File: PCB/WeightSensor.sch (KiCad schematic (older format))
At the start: 2 parts

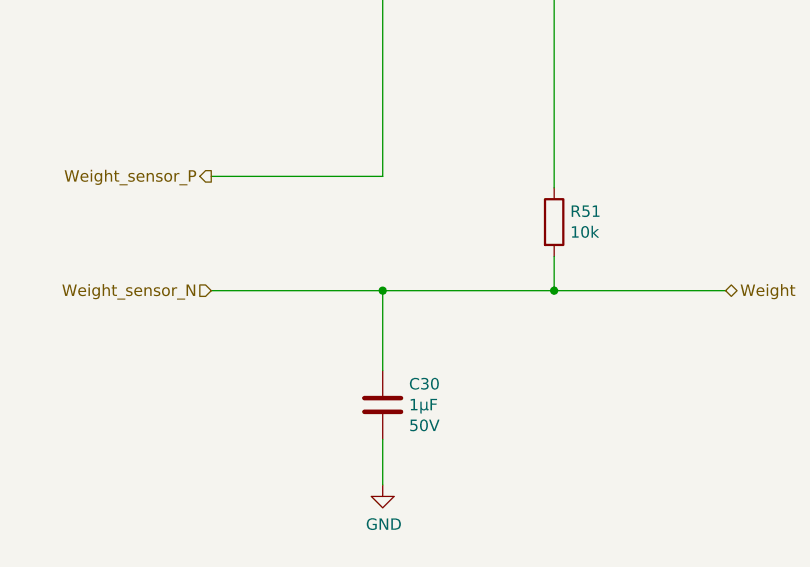
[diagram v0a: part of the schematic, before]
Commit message: Add support for the hall sensors and dome LED
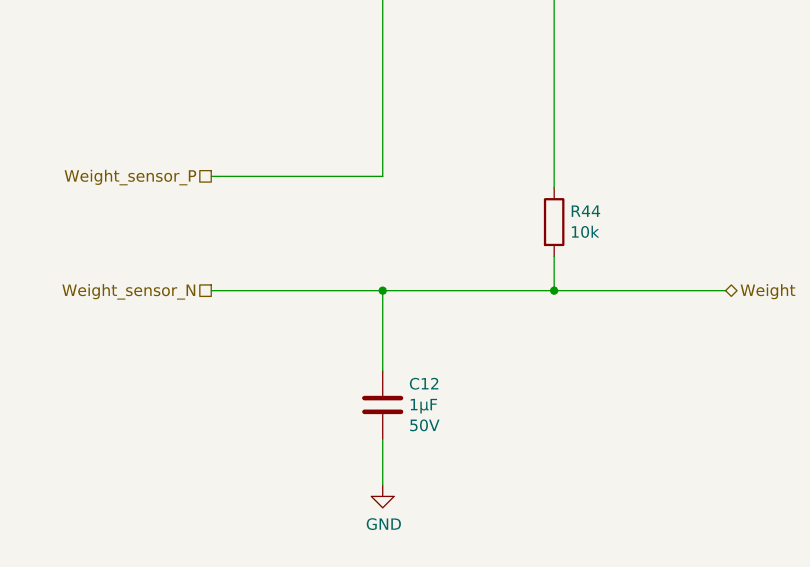
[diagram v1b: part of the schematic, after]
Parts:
- renumbered C30 to C12, R51 to R44
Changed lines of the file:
@@
 $Descr A4 11693 8268
 encoding utf-8
-Sheet 20 20
+Sheet 17 22
 Title "Litter Robot 3 - Weight sensor"
-Date "2021-04-02"
+Date "2021-04-03"
 Rev "A1"
 Comp "L. Sartory"
@@
 Comment4 ""
 $EndDescr
-Text HLabel 5000 4000 0    50   Input ~ 0
+Text HLabel 5000 4000 0    50   UnSpc ~ 0
 Weight_sensor_N
 $Comp
@@
 AR Path="/603F1DCE/606BBD2A" Ref="#PWR?"  Part="1"
 AR Path="/60624089/606BBD2A" Ref="#PWR?"  Part="1"
-AR Path="/606A580A/606BBD2A" Ref="#PWR0113"  Part="1"
-F 0 "#PWR0113" H 5750 4600 50  0001 C CNN
+AR Path="/606A580A/606BBD2A" Ref="#PWR071"  Part="1"
+F 0 "#PWR071" H 5750 4600 50  0001 C CNN
 F 1 "GND" H 5755 4677 50  0000 C CNN
 F 2 "" H 5750 4850 50  0001 C CNN
@@
 AR Path="/603F1DCE/606BBD37" Ref="R?"  Part="1"
 AR Path="/60624089/606BBD37" Ref="R?"  Part="1"
-AR Path="/606A580A/606BBD37" Ref="R51"  Part="1"
-F 0 "R51" H 6570 3746 50  0000 L CNN
+AR Path="/606A580A/606BBD37" Ref="R44"  Part="1"
+F 0 "R44" H 6570 3746 50  0000 L CNN
 F 1 "10k" H 6570 3655 50  0000 L CNN
 F 2 "Resistor_SMD:R_0603_1608Metric" V 6430 3700 50  0001 C CNN
@@
 Text HLabel 7250 4000 2    50   3State ~ 0
 Weight
-Text HLabel 5000 3500 0    50   Output ~ 0
+Text HLabel 5000 3500 0    50   UnSpc ~ 0
 Weight_sensor_P
 Text Notes 750  7500 0    50   ~ 0
@@
 AR Path="/603F1DCE/60701378" Ref="C?"  Part="1"
 AR Path="/60624089/60701378" Ref="C?"  Part="1"
-AR Path="/606A580A/60701378" Ref="C30"  Part="1"
-F 0 "C30" H 5865 4591 50  0000 L CNN
+AR Path="/606A580A/60701378" Ref="C12"  Part="1"
+F 0 "C12" H 5865 4591 50  0000 L CNN
 F 1 "1µF" H 5865 4500 50  0000 L CNN
 F 2 "Capacitor_SMD:C_0603_1608Metric" H 5788 4350 50  0001 C CNN

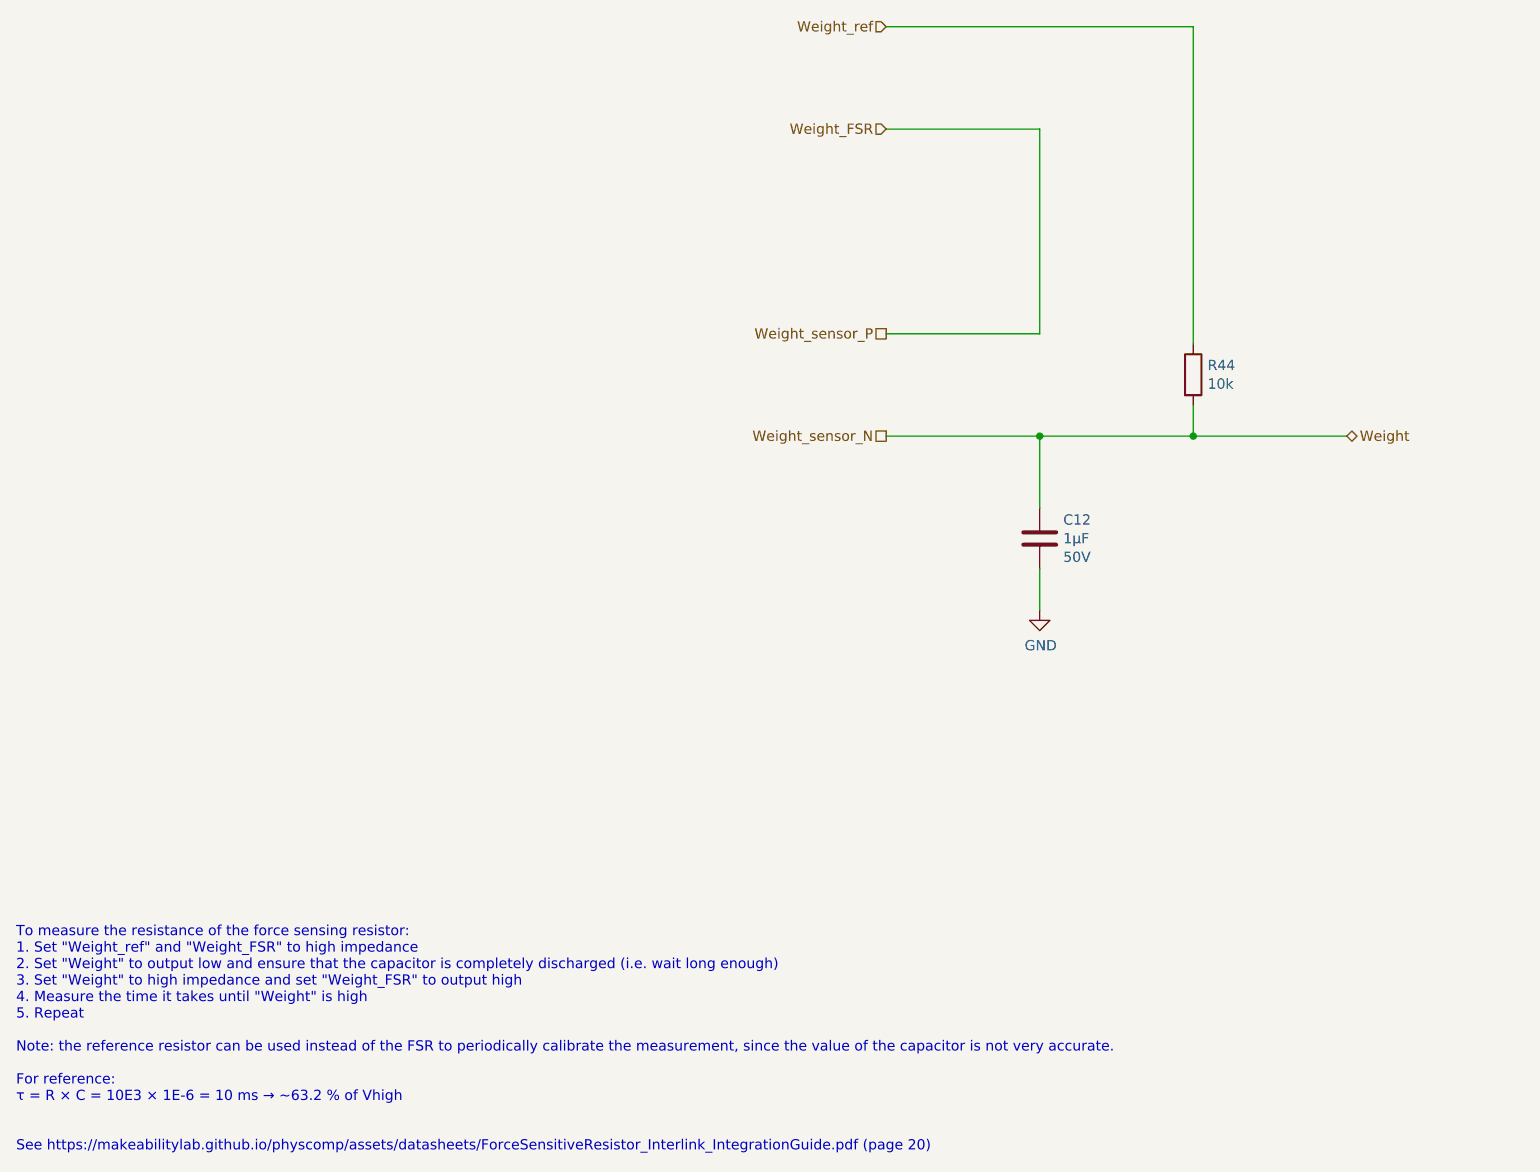
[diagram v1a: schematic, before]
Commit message: Reduce the weight sensor capacitor value
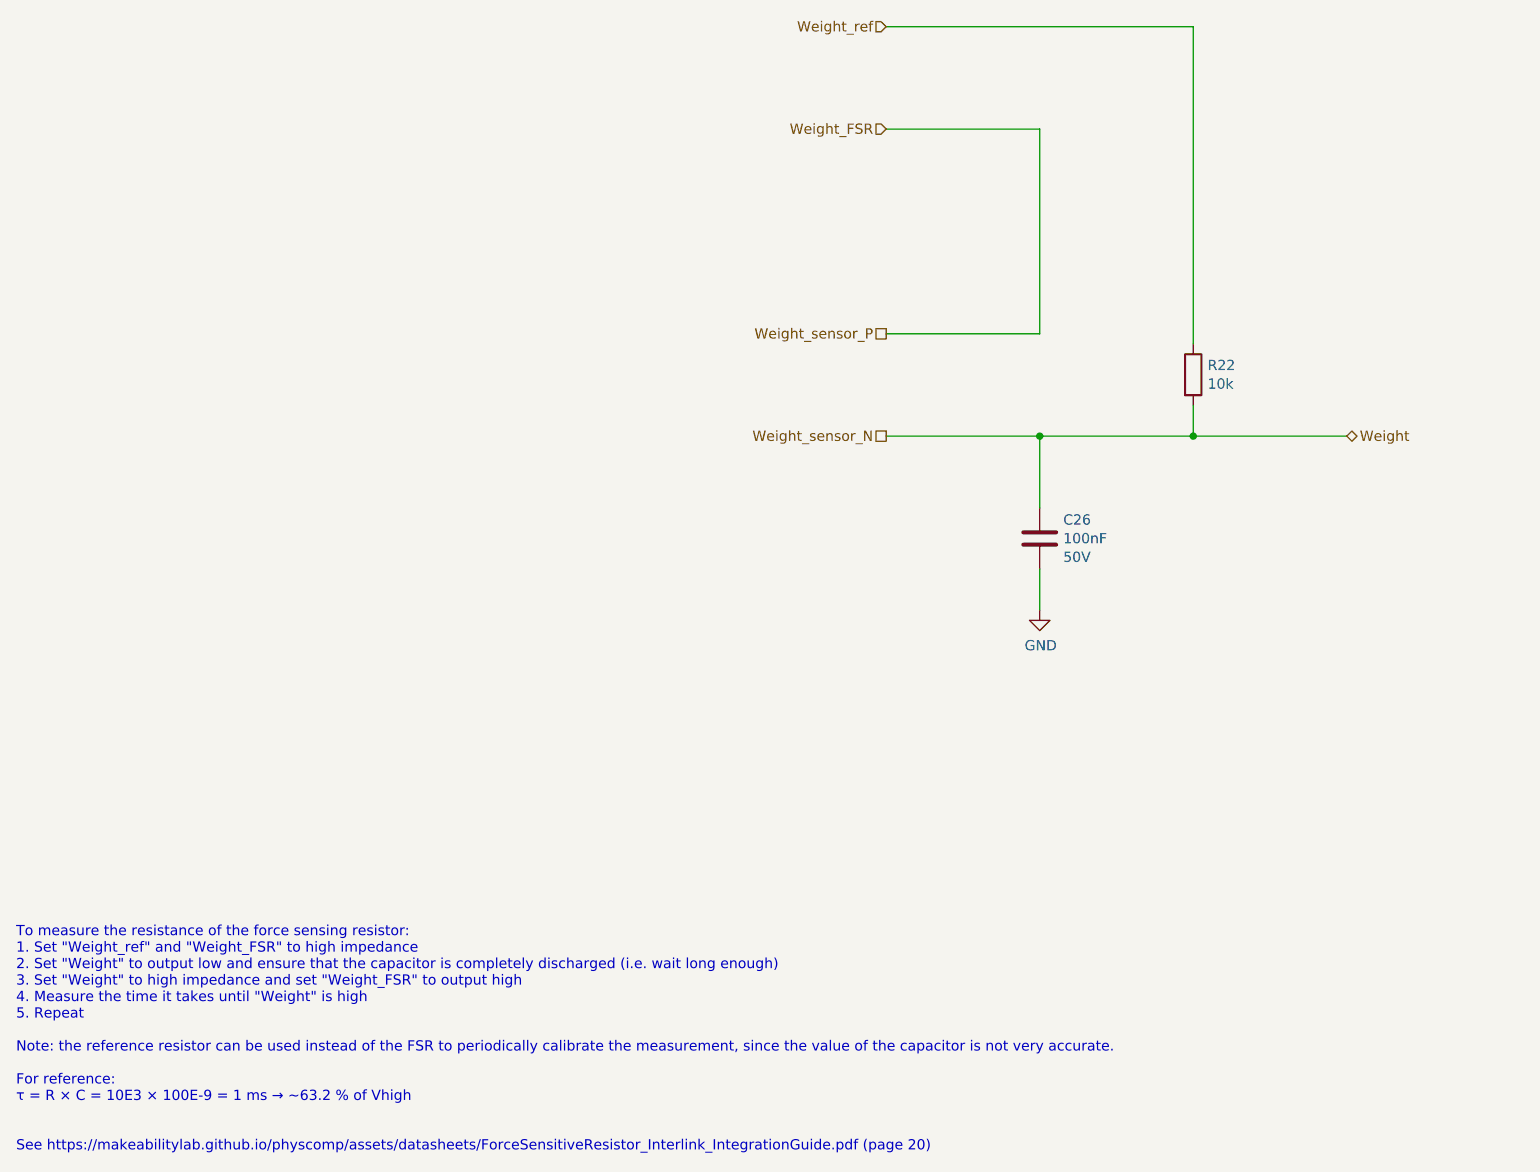
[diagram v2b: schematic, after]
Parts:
- removed C12: 1µF, Capacitor_SMD:C_0603_1608Metric, symbol Device:C
- added C26: 100nF, Capacitor_SMD:C_0603_1608Metric, symbol Device:C
- renumbered R44 to R22
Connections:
- net GND: now also C26.2
- net Weight: now also C26.1
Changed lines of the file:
@@
 $Descr A4 11693 8268
 encoding utf-8
-Sheet 17 22
+Sheet 6 22
 Title "Litter Robot 3 - Weight sensor"
-Date "2021-04-03"
+Date "2021-04-05"
 Rev "A1"
 Comp "L. Sartory"
@@
 AR Path="/603F1DCE/606BBD2A" Ref="#PWR?"  Part="1"
 AR Path="/60624089/606BBD2A" Ref="#PWR?"  Part="1"
-AR Path="/606A580A/606BBD2A" Ref="#PWR071"  Part="1"
-F 0 "#PWR071" H 5750 4600 50  0001 C CNN
+AR Path="/606A580A/606BBD2A" Ref="#PWR070"  Part="1"
+F 0 "#PWR070" H 5750 4600 50  0001 C CNN
 F 1 "GND" H 5755 4677 50  0000 C CNN
 F 2 "" H 5750 4850 50  0001 C CNN
@@
 AR Path="/603F1DCE/606BBD37" Ref="R?"  Part="1"
 AR Path="/60624089/606BBD37" Ref="R?"  Part="1"
-AR Path="/606A580A/606BBD37" Ref="R44"  Part="1"
-F 0 "R44" H 6570 3746 50  0000 L CNN
+AR Path="/606A580A/606BBD37" Ref="R22"  Part="1"
+F 0 "R22" H 6570 3746 50  0000 L CNN
 F 1 "10k" H 6570 3655 50  0000 L CNN
 F 2 "Resistor_SMD:R_0603_1608Metric" V 6430 3700 50  0001 C CNN
@@
 Weight_sensor_P
 Text Notes 750  7500 0    50   ~ 0
-To measure the resistance of the force sensing resistor:\n1. Set "Weight_ref" and "Weight_FSR" to high impedance\n2. Set "Weight" to output low and ensure that the capacitor is completely discharged (i.e. wait long enough)\n3. Set "Weight" to high impedance and set "Weight_FSR" to output high\n4. Measure the time it takes until "Weight" is high\n5. Repeat\n\nNote: the reference resistor can be used instead of the FSR to periodically calibrate the measurement, since the value of the capacitor is not very accurate.\n\nFor reference:\nτ = R × C = 10E3 × 1E-6 = 10 ms → ~~63.2 % of Vhigh\n\n\nSee https://makeabilitylab.github.io/physcomp/assets/datasheets/ForceSensitiveResistor_Interlink_IntegrationGuide.pdf (page 20)
+To measure the resistance of the force sensing resistor:\n1. Set "Weight_ref" and "Weight_FSR" to high impedance\n2. Set "Weight" to output low and ensure that the capacitor is completely discharged (i.e. wait long enough)\n3. Set "Weight" to high impedance and set "Weight_FSR" to output high\n4. Measure the time it takes until "Weight" is high\n5. Repeat\n\nNote: the reference resistor can be used instead of the FSR to periodically calibrate the measurement, since the value of the capacitor is not very accurate.\n\nFor reference:\nτ = R × C = 10E3 × 100E-9 = 1 ms → ~~63.2 % of Vhigh\n\n\nSee https://makeabilitylab.github.io/physcomp/assets/datasheets/ForceSensitiveResistor_Interlink_IntegrationGuide.pdf (page 20)
+Wire Wire Line
+	5750 4650 5750 4850
 $Comp
 L Device:C C?
-U 1 1 60701378
+U 1 1 606BC432
 P 5750 4500
-AR Path="/603F20AB/60701378" Ref="C?"  Part="1"
-AR Path="/603F1DCE/60701378" Ref="C?"  Part="1"
-AR Path="/60624089/60701378" Ref="C?"  Part="1"
-AR Path="/606A580A/60701378" Ref="C12"  Part="1"
-F 0 "C12" H 5865 4591 50  0000 L CNN
-F 1 "1µF" H 5865 4500 50  0000 L CNN
+AR Path="/603F20AB/606BC432" Ref="C?"  Part="1"
+AR Path="/60624089/606BC432" Ref="C?"  Part="1"
+AR Path="/603F1F4D/606BC432" Ref="C?"  Part="1"
+AR Path="/603F1F4D/60647CC2/606BC432" Ref="C?"  Part="1"
+AR Path="/603F1F4D/60659E39/606BC432" Ref="C?"  Part="1"
+AR Path="/606A580A/606BC432" Ref="C26"  Part="1"
+F 0 "C26" H 5865 4591 50  0000 L CNN
+F 1 "100nF" H 5865 4500 50  0000 L CNN
 F 2 "Capacitor_SMD:C_0603_1608Metric" H 5788 4350 50  0001 C CNN
 F 3 "https://product.tdk.com/system/files/dam/doc/product/capacitor/ceramic/mlcc/catalog/mlcc_commercial_general_en.pdf" H 5750 4500 50  0001 C CNN
 F 4 "50V" H 5865 4409 50  0000 L CNN "Voltage"
-F 5 "C1608X5R1H105K080AB" H 5750 4500 50  0001 C CNN "Part_number"
+F 5 "C1608X5R1H104K080AA" H 5750 4500 50  0001 C CNN "Part_number"
 	1    5750 4500
 	1    0    0    -1
 $EndComp
 Wire Wire Line
-	5750 4650 5750 4850
-Wire Wire Line
 	5750 4000 5750 4350

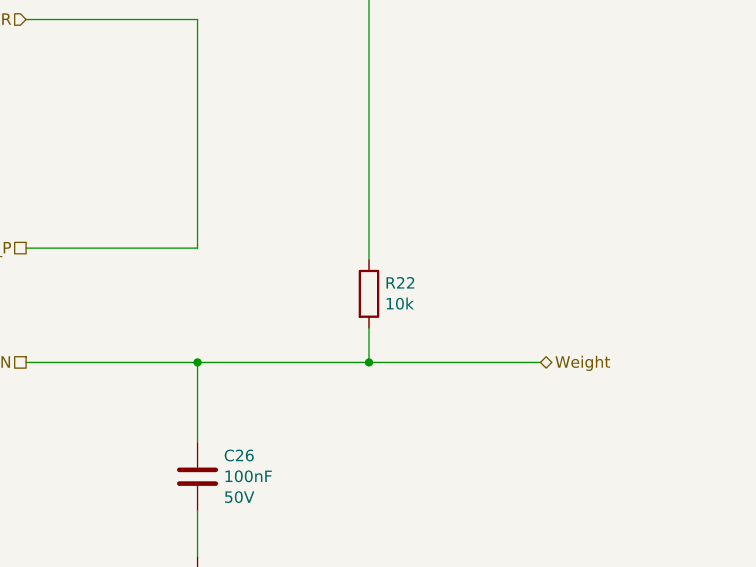
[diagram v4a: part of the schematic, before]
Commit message: Add jumpers on the power supply outputs
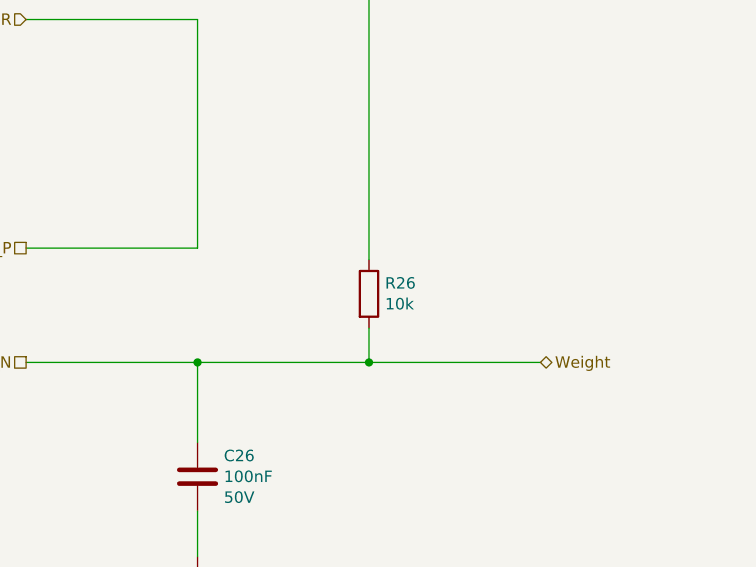
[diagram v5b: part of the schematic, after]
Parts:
- renumbered R22 to R26
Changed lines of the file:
@@
 Sheet 7 23
 Title "Litter Robot 3 - Weight sensor"
-Date "2021-04-10"
+Date "2021-05-24"
 Rev "A1"
 Comp "L. Sartory"
@@
 AR Path="/603F1DCE/606BBD37" Ref="R?"  Part="1"
 AR Path="/60624089/606BBD37" Ref="R?"  Part="1"
-AR Path="/606A580A/606BBD37" Ref="R22"  Part="1"
-F 0 "R22" H 6570 3746 50  0000 L CNN
+AR Path="/606A580A/606BBD37" Ref="R26"  Part="1"
+F 0 "R26" H 6570 3746 50  0000 L CNN
 F 1 "10k" H 6570 3655 50  0000 L CNN
 F 2 "Resistor_SMD:R_0603_1608Metric" V 6430 3700 50  0001 C CNN
